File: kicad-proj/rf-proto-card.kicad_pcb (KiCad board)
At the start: 2 copper layers, 85.6 x 54 mm, 4 parts

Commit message: layout done
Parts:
- added A1: R, Resistor_SMD:R_0603_1608Metric, F.Cu at (134.0, 79.8)
- added A10: R, Resistor_SMD:R_0603_1608Metric, F.Cu at (153.0, 82.0)
- added A11: R, Resistor_SMD:R_0603_1608Metric, F.Cu at (153.0, 85.0)
- added A12: R, Resistor_SMD:R_0603_1608Metric, F.Cu at (156.0, 79.8)
- added A13: R, Resistor_SMD:R_0603_1608Metric, F.Cu at (156.0, 84.2)
- added A14: R, Resistor_SMD:R_0603_1608Metric, F.Cu at (158.0, 79.8)
- added A2: R, Resistor_SMD:R_0603_1608Metric, F.Cu at (136.0, 79.8)
- added A3: R, Resistor_SMD:R_0603_1608Metric, F.Cu at (136.0, 84.2)
- added A4: R, Resistor_SMD:R_0603_1608Metric, F.Cu at (139.0, 82.0)
- added A5: R, Resistor_SMD:R_0603_1608Metric, F.Cu at (139.0, 85.0)
- added A6: R, Resistor_SMD:R_0603_1608Metric, F.Cu at (142.0, 79.8)
- added A7: R, Resistor_SMD:R_0603_1608Metric, F.Cu at (142.0, 84.2)
- added A8: R, Resistor_SMD:R_0603_1608Metric, F.Cu at (150.0, 79.8)
- added A9: R, Resistor_SMD:R_0603_1608Metric, F.Cu at (150.0, 84.2)
- added B1: R, Resistor_SMD:R_0603_1608Metric, F.Cu at (158.0, 108.4)
- added B10: R, Resistor_SMD:R_0603_1608Metric, F.Cu at (139.0, 106.2)
- added B11: R, Resistor_SMD:R_0603_1608Metric, F.Cu at (139.0, 103.2)
- added B12: R, Resistor_SMD:R_0603_1608Metric, F.Cu at (136.0, 108.4)
- added B13: R, Resistor_SMD:R_0603_1608Metric, F.Cu at (136.0, 104.1)
- added B14: R, Resistor_SMD:R_0603_1608Metric, F.Cu at (134.0, 108.4)
- added B2: R, Resistor_SMD:R_0603_1608Metric, F.Cu at (156.0, 108.4)
- added B3: R, Resistor_SMD:R_0603_1608Metric, F.Cu at (156.0, 104.1)
- added B4: R, Resistor_SMD:R_0603_1608Metric, F.Cu at (153.0, 106.2)
- added B5: R, Resistor_SMD:R_0603_1608Metric, F.Cu at (153.0, 103.2)
- added B6: R, Resistor_SMD:R_0603_1608Metric, F.Cu at (150.0, 108.4)
- added B7: R, Resistor_SMD:R_0603_1608Metric, F.Cu at (150.0, 104.1)
- added B8: R, Resistor_SMD:R_0603_1608Metric, F.Cu at (142.0, 108.4)
- added B9: R, Resistor_SMD:R_0603_1608Metric, F.Cu at (142.0, 104.1)
- added J1: sma-a-in, Connector_Coaxial:SMA_Amphenol_132134-10_Vertical, F.Cu at (107.0, 85.0)
- added J2: sma-b-in, Connector_Coaxial:SMA_Amphenol_132134-10_Vertical, F.Cu at (184.6, 103.2)
- added J3: sma-a-out, Connector_Coaxial:SMA_Amphenol_132134-10_Vertical, F.Cu at (184.6, 85.0)
- added J4: sma-b-out, Connector_Coaxial:SMA_Amphenol_132134-10_Vertical, F.Cu at (107.0, 103.2)
- added J5: RF_Shield_One_Piece, RF_Shielding:Laird_Technologies_BMI-S-209-F_29.36x18.50mm, F.Cu at (146.0, 82.0)
- added J6: RF_Shield_One_Piece, RF_Shielding:Laird_Technologies_BMI-S-209-F_29.36x18.50mm, F.Cu at (146.0, 106.2)
- added TP1: rail-a-in, TestPoint:TestPoint_Pad_D1.0mm, F.Cu at (127.0, 79.0)
- added TP2: gnd, TestPoint:TestPoint_Pad_D1.0mm, F.Cu at (127.0, 72.8)
- added TP3: rail-b-in, TestPoint:TestPoint_Pad_D1.0mm, F.Cu at (165.0, 109.2)
- added TP4: gnd, TestPoint:TestPoint_Pad_D1.0mm, F.Cu at (165.0, 115.5)
- added TP5: rail-a-out, TestPoint:TestPoint_Pad_D1.0mm, F.Cu at (165.0, 79.0)
- added TP6: gnd, TestPoint:TestPoint_Pad_D1.0mm, F.Cu at (165.0, 72.8)
- added TP7: rail-b-out, TestPoint:TestPoint_Pad_D1.0mm, F.Cu at (127.0, 109.2)
- added TP8: gnd, TestPoint:TestPoint_Pad_D1.0mm, F.Cu at (127.0, 115.5)
- added U1: GALI-52, Package_TO_SOT_SMD:SOT-89-3, F.Cu at (146.0, 83.3)
- added U2: GALI-52, Package_TO_SOT_SMD:SOT-89-3, F.Cu at (146.0, 104.9)
- added Z1: proto-area, rf-proto-card:proto-area, F.Cu at (119.8, 74.8)
- added Z2: proto-area, rf-proto-card:proto-area, F.Cu at (172.2, 113.2)
- added Z3: proto-area, rf-proto-card:proto-area, F.Cu at (119.8, 113.2)
- added Z4: proto-area, rf-proto-card:proto-area, F.Cu at (172.2, 74.8)
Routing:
- net Net-(B3-Pad1): track 0.00 -> 31.0 mm
- net Net-(B11-Pad2): track 0.00 -> 31.0 mm
- net Net-(A3-Pad1): track 0.00 -> 31.0 mm
- net Net-(A11-Pad1): track 0.00 -> 30.5 mm
- net Net-(B14-Pad2): track 0.00 -> 7.00 mm
- net Net-(B1-Pad2): track 0.00 -> 7.00 mm
- net Net-(A14-Pad2): track 0.00 -> 7.00 mm
- net Net-(A1-Pad2): track 0.00 -> 7.00 mm
- net Net-(B10-Pad2): track 0.00 -> 6.50 mm
- net Net-(B1-Pad1): track 0.00 -> 6.50 mm
- net Net-(A10-Pad1): track 0.00 -> 6.50 mm
- net Net-(A1-Pad1): track 0.00 -> 6.50 mm
- net Net-(A10-Pad2): track 0.00 -> 4.60 mm
- net Net-(B10-Pad1): track 0.00 -> 4.50 mm
- net Net-(B5-Pad2): track 0.00 -> 4.41 mm
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- added copper zone on B.Cu, net GND
- added copper zone on F.Cu, net GND
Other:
- net class Default: clearance 0.2 -> 0.26; trace_width 0.25 -> 0.95; via_dia 0.8 -> 0.7; via_drill 0.4 -> 0.3
- rule trace_clearance: 0.2 -> 0.26
- board text added: "Shield p/n: Laird BMI-S-209-F"

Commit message: Complete and gerber exported
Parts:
- added FID1: card-info-gold, rf-proto-card:front-info-gold, B.Cu at (146.0, 94.0)
- added FID2: card-info-white, rf-proto-card:front-info-white, B.Cu at (146.0, 94.0)
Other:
- net class Default: via_dia 0.7 -> 0.5; via_drill 0.3 -> 0.25
- rule via_min_drill: 0.3 -> 0.2
- board text added: "50 ohm"
- board text added: "Microwave & RF Proto Card"
- board text added: "a (in)"
- board text added: "b (out)"
- board text added: "c (in)"
- board text added: "d (out)"
- board text added: "gnd"
- board text added: "https://github.com/siliconwitchery/rf-proto-card.git"
- board text added: "proto area"
- board text added: "vb-a"
- board text added: "vb-b"
- board text added: "vb-c"
- board text added: "vb-d"
- board text removed: "Shield p/n: Laird BMI-S-209-F"

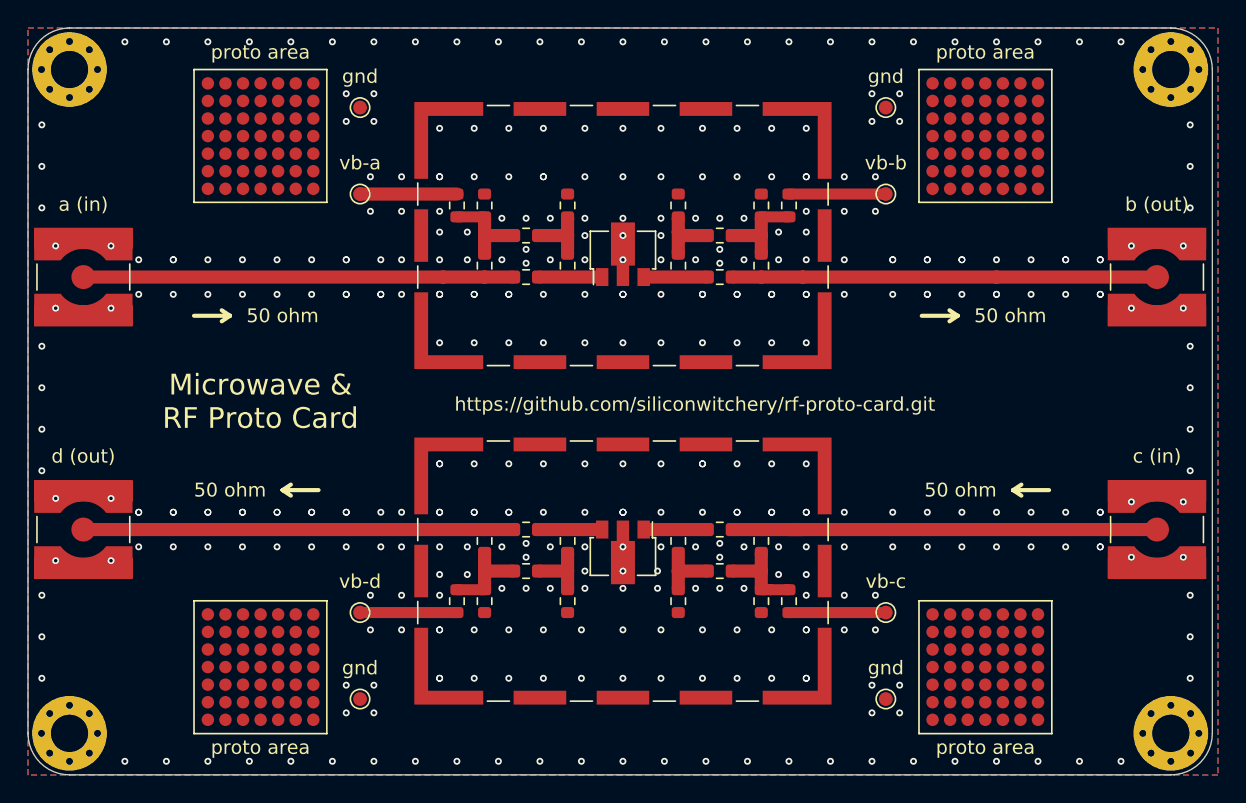
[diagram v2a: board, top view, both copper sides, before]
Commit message: Updated PCB to correct board core thickness of 0.711mm
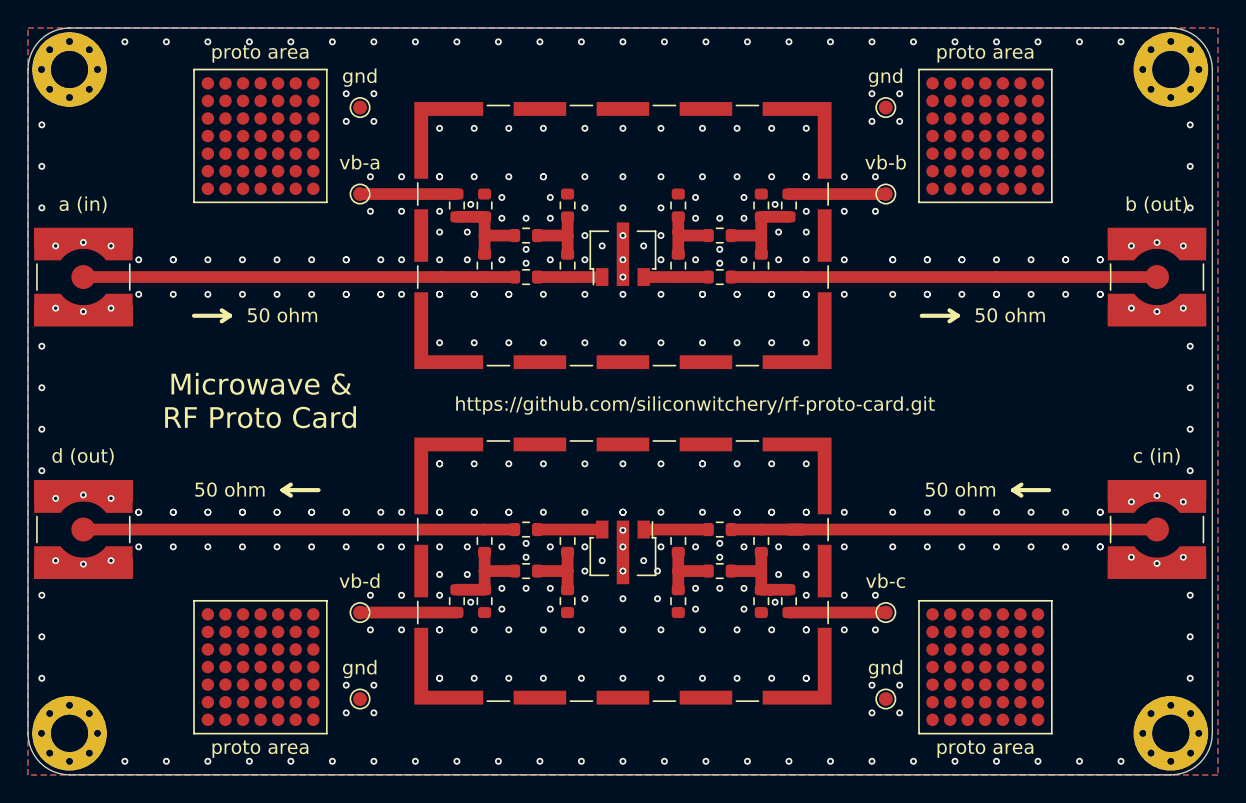
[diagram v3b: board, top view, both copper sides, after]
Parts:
- J2: renamed from J1; value sma-a-in -> sma-a
- J3: value sma-a-out -> sma-b
- J5: renamed from J2; value sma-b-in -> sma-c
- J6: renamed from J4; value sma-b-out -> sma-d
- TP1: value rail-a-in -> vbias-a
- TP2: renamed from TP5; value rail-a-out -> vbias-b
- TP5: renamed from TP3; value rail-b-in -> vbias-c
- TP6: renamed from TP7; value rail-b-out -> vbias-d
- U1, U2: footprint Package_TO_SOT_SMD:SOT-89-3 -> rf-proto-card:SOT-89-3
- renumbered A6 to A3, A3 to A5, A7 to A6, A5 to A7, A8 to B1, A12 to B2, A14 to B3, A10 to B4, A9 to B5, A13 to B6, A11 to B7, B1 to C1, B2 to C2, B6 to C3, B4 to C4, B3 to C5, B7 to C6, B5 to C7, B8 to D1, B12 to D2, B14 to D3, B10 to D4, B9 to D5, B13 to D6, B11 to D7, J5 to J1, J6 to J4, TP2 to TP3, TP6 to TP4, TP4 to TP7
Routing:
- net GND: vias 388 -> 412
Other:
- net class Default: clearance 0.26 -> 0.211; trace_width 0.95 -> 0.85
- rule trace_clearance: 0.26 -> 0.211
- rule trace_min: 0.2 -> 0.85

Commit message: Migrated to KiCad 6
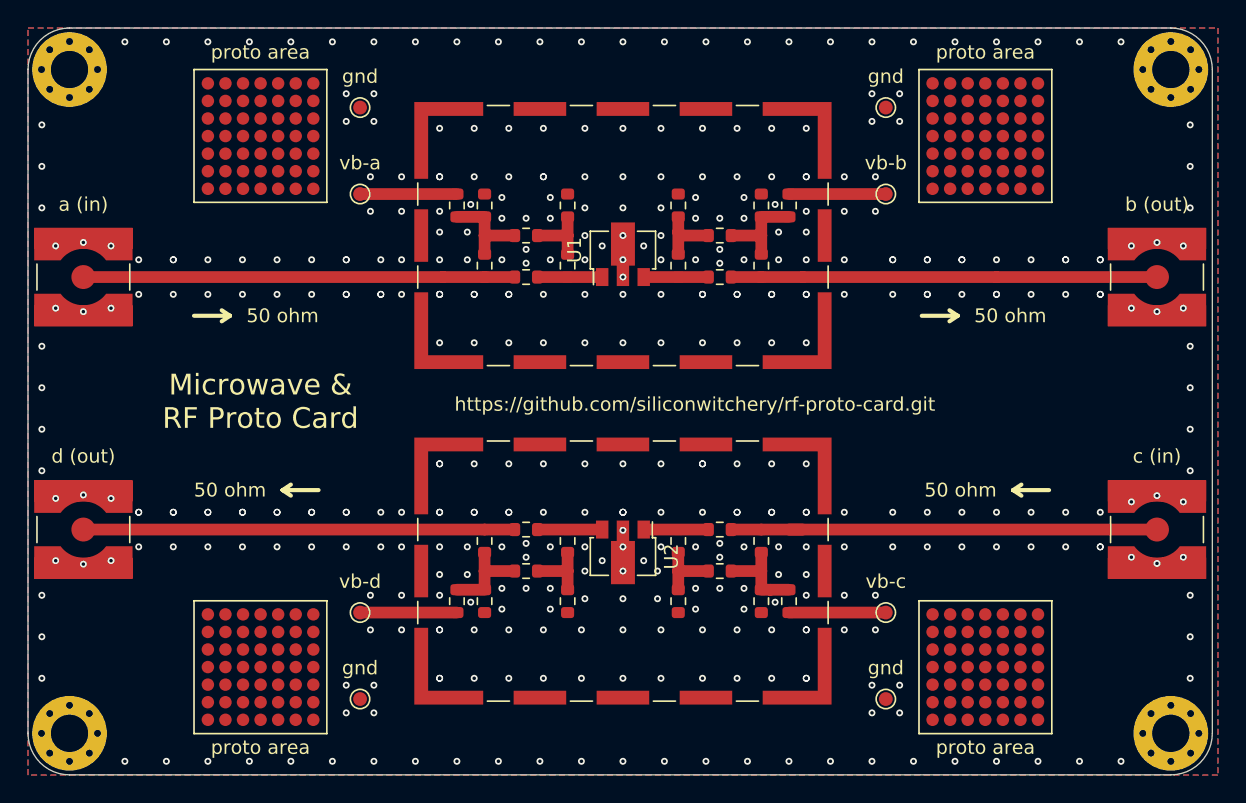
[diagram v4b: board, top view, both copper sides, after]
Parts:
- U1, U2: footprint rf-proto-card:SOT-89-3 -> Package_TO_SOT_SMD:SOT-89-3
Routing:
- net GND: vias 412 -> 411
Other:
- net class Default removed
